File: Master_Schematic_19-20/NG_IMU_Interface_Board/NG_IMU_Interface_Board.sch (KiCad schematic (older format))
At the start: 34 parts, among them J1 Conn_01x04, J2 Conn_01x02, J3 Conn_01x10, J4 Conn_01x03, J5 Conn_02x12_Top_Bottom, J6 GS2, J7 GS2, J8 Conn_01x01, U1 PYB30-Q24-T515, U2 MAX3280EAUK+T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

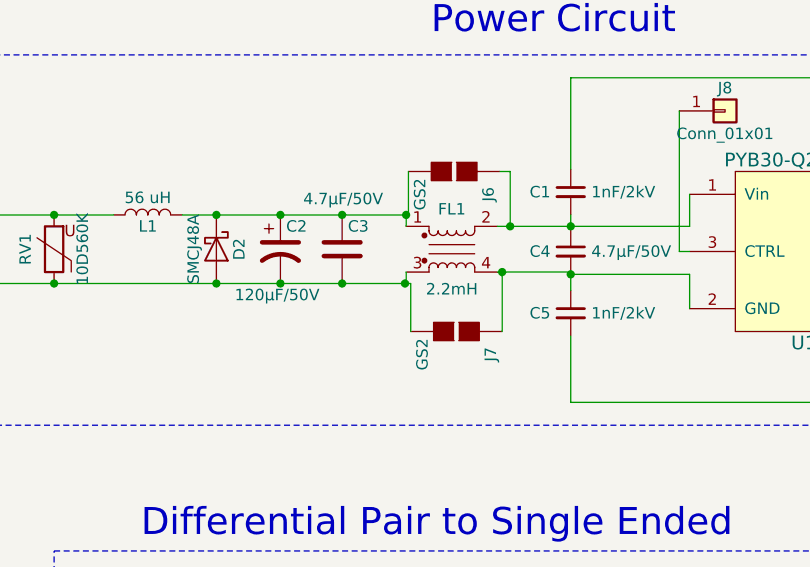
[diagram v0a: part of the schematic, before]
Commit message: Added emergency stop button and cleaned up IMU interface board
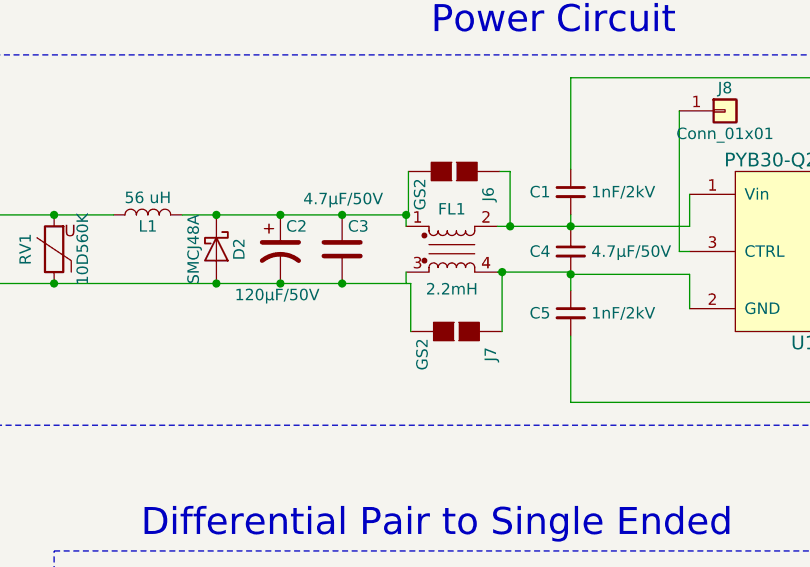
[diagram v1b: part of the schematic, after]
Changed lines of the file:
@@
 Comment4 ""
 $EndDescr
-Text Label 2960 2370 2    60   ~ 0
-+12V
-$Comp
-L Connector_Generic:Conn_01x02 J2
-U 1 1 5AC98297
-P 3240 2370
-F 0 "J2" H 3240 2470 50  0000 C CNN
-F 1 "Conn_01x02" H 3240 2170 50  0000 C CNN
-F 2 "Connectors_Molex:Molex_MegaFit_2x01x5.70mm_Angled" H 3240 2370 50  0001 C CNN
-F 3 "" H 3240 2370 50  0001 C CNN
-	1    3240 2370
-	1    0    0    -1
-$EndComp
 $Comp
 L Device:Varistor RV1
@@
 Text Notes 2890 6070 2    118  ~ 0
 Test Points
-Text Label 3990 2590 2    59   ~ 0
-gnd
 $Comp
 L NG_IMU_Interface_Board-rescue:GS2 J6
@@
 $EndComp
 Wire Wire Line
-	2960 2370 3040 2370
-Wire Wire Line
-	2870 2470 3040 2470
-Wire Wire Line
 	4100 2290 4400 2290
 Wire Wire Line
@@
 Wire Wire Line
 	5960 2800 5960 2590
-Connection ~ 5935 2590
 Wire Wire Line
 	6360 2800 6360 2540
@@
 Wire Wire Line
 	6360 2540 6660 2540
-Wire Wire Line
-	5660 2590 5960 2590
 Text Label 2840 7070 0    59   ~ 0
 CLK_clean
+Wire Wire Line
+	5660 2590 5960 2590
+Text Label 3990 2590 2    59   ~ 0
+gnd
 Text Label 2870 2470 2    59   ~ 0
 gnd
+Wire Wire Line
+	2870 2470 3040 2470
+Wire Wire Line
+	2960 2370 3040 2370
+$Comp
+L Connector_Generic:Conn_01x02 J2
+U 1 1 5AC98297
+P 3240 2370
+F 0 "J2" H 3240 2470 50  0000 C CNN
+F 1 "Conn_01x02" H 3240 2170 50  0000 C CNN
+F 2 "Connectors_Molex:Molex_MegaFit_2x01x5.70mm_Angled" H 3240 2370 50  0001 C CNN
+F 3 "" H 3240 2370 50  0001 C CNN
+	1    3240 2370
+	1    0    0    -1
+$EndComp
+Text Label 2960 2370 2    60   ~ 0
++12V
 $EndSCHEMATC

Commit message: IMU Interface Board updates and improvements and general cleanup
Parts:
- removed U3: MAX3280EAUK+T, TO_SOT_Packages_SMD:SOT-23-5_HandSoldering, symbol NG_IMU_Interface_Board-rescue:MAX3280EAUK+T
- added U3: MAX3280EAUK+T, Package_TO_SOT_SMD:SOT-23-5_HandSoldering, symbol NG_IMU_Components:MAX3280EAUK+T
- J6, J7: symbol NG_IMU_Interface_Board-rescue:GS2 -> NG_IMU_Components:GS2
- U1: symbol NG_IMU_Interface_Board-rescue:PYB30-Q24-T515 -> NG_IMU_Components:PYB30-Q24-T515
- U2: footprint TO_SOT_Packages_SMD:SOT-23-5_HandSoldering -> Package_TO_SOT_SMD:SOT-23-5_HandSoldering; symbol NG_IMU_Interface_Board-rescue:MAX3280EAUK+T -> NG_IMU_Components:MAX3280EAUK+T
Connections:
- wire segments 71 -> 80
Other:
- moved on the sheet: J4, R2, R3, U2
